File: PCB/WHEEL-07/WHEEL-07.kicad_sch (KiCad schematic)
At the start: 26 parts, among them J1 Conn_01x06_Male, J11 DBG, U1 STM32F405RGTx, Y1 16Mhz, Y2 32KHz

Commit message: Changed connectors setup
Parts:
- removed Y1: 16Mhz, Crystal:Crystal_SMD_5032-2Pin_5.0x3.2mm, symbol Device:Crystal_Small
- added H1, H2, H3, H4: MountingHole, MountingHole:MountingHole_2.2mm_M2, symbol Mechanical:MountingHole
- added Y1: 16Mhz, Crystal:Crystal_SMD_2016-4Pin_2.0x1.6mm, symbol Device:Crystal_GND24_Small
- C1, C2, C3, C34, C35, C36, C37, C4, C5, C6, C7, C8: footprint Capacitor_SMD:C_0402_1005Metric -> Capacitor_SMD:C_0402_1005Metric_Pad0.74x0.62mm_HandSolder
- C33: footprint Capacitor_SMD:C_0201_0603Metric -> Capacitor_SMD:C_0603_1608Metric
- L1: footprint (none) -> Inductor_SMD:L_0402_1005Metric
- R1, R2, R3, R5: footprint Resistor_SMD:R_0402_1005Metric -> Resistor_SMD:R_0402_1005Metric_Pad0.72x0.64mm_HandSolder
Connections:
- net CAN1_TERMINATOR_SW: now also U1.56 (PB4); no longer U1.59 (PB7)
- net CAN2_TERMINATOR_SW: now also U1.59 (PB7); no longer U1.56 (PB4)
- net GND: now also Y1.2, Y1.4
- net OSC_IN: now also Y1.1
- net OSC_OUT: now also Y1.3
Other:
- note added: "39uH"

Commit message: Finished layout
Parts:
- removed H2, H3, H4: MountingHole, MountingHole:MountingHole_2.2mm_M2, symbol Mechanical:MountingHole
- J1: footprint (none) -> Connector_Molex:Molex_Micro-Latch_53254-0670_1x06_P2.00mm_Horizontal
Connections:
- net CAN_BUS/CAN1_H: now also J1.3 (Pin_3); no longer J1.2 (Pin_2)
- net CAN_BUS/CAN1_L: now also J1.4 (Pin_4); no longer J1.1 (Pin_1)
- net CAN_BUS/CAN2_H: now also J1.5 (Pin_5); no longer J1.4 (Pin_4)
- net CAN_BUS/CAN2_L: now also J1.6 (Pin_6); no longer J1.3 (Pin_3)
- net GND: now also J1.1 (Pin_1); no longer J1.6 (Pin_6)
- net +12V: no longer names the net of J11.3 (Pin_3)
- net +12V: no longer J1.5 (Pin_5)
- net CAN1_TERMINATOR_SW: no longer names the net of U1.56 (PB4)
- net CAN2_TERMINATOR_SW: no longer names the net of U1.59 (PB7)
- new net 12V_CONN: J1.2 (Pin_2)
- no-connect marks 7 -> 11
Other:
- sheet CAN_BUS ports: added none; removed CAN_TERMINATOR_1, CAN_TERMINATOR_2

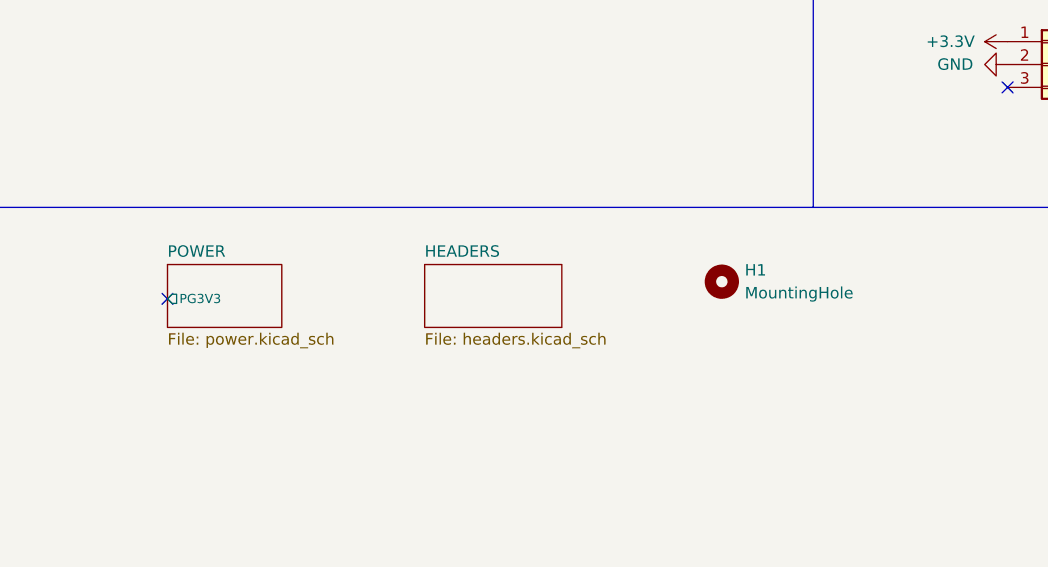
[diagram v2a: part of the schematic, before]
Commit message: Changed power supply section for 2 x LDO40
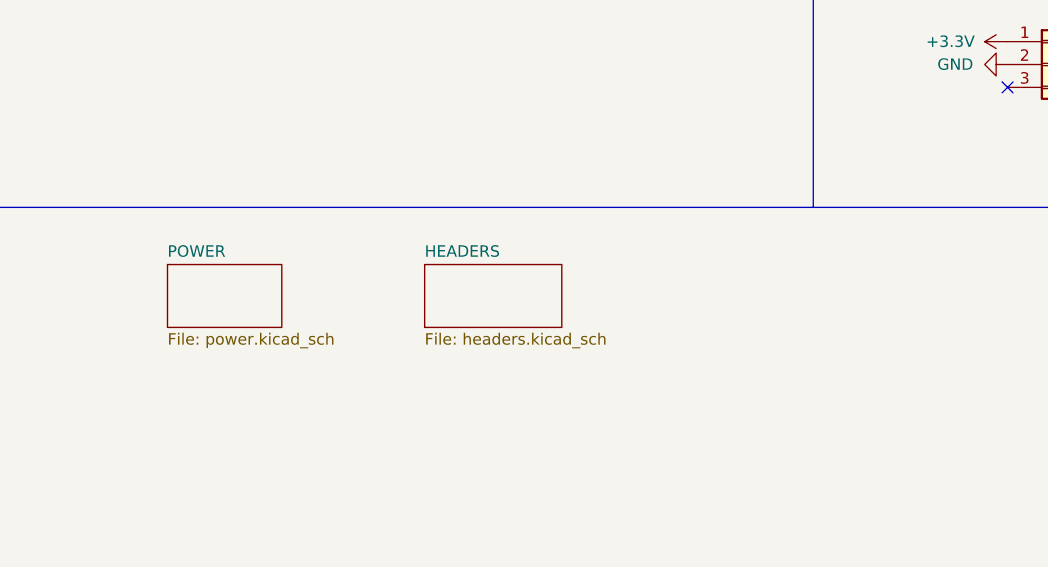
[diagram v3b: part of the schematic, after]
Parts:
- removed H1: MountingHole, MountingHole:MountingHole_2.2mm_M2, symbol Mechanical:MountingHole
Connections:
- no-connect marks 11 -> 10
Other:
- sheet POWER ports: added none; removed PG3V3

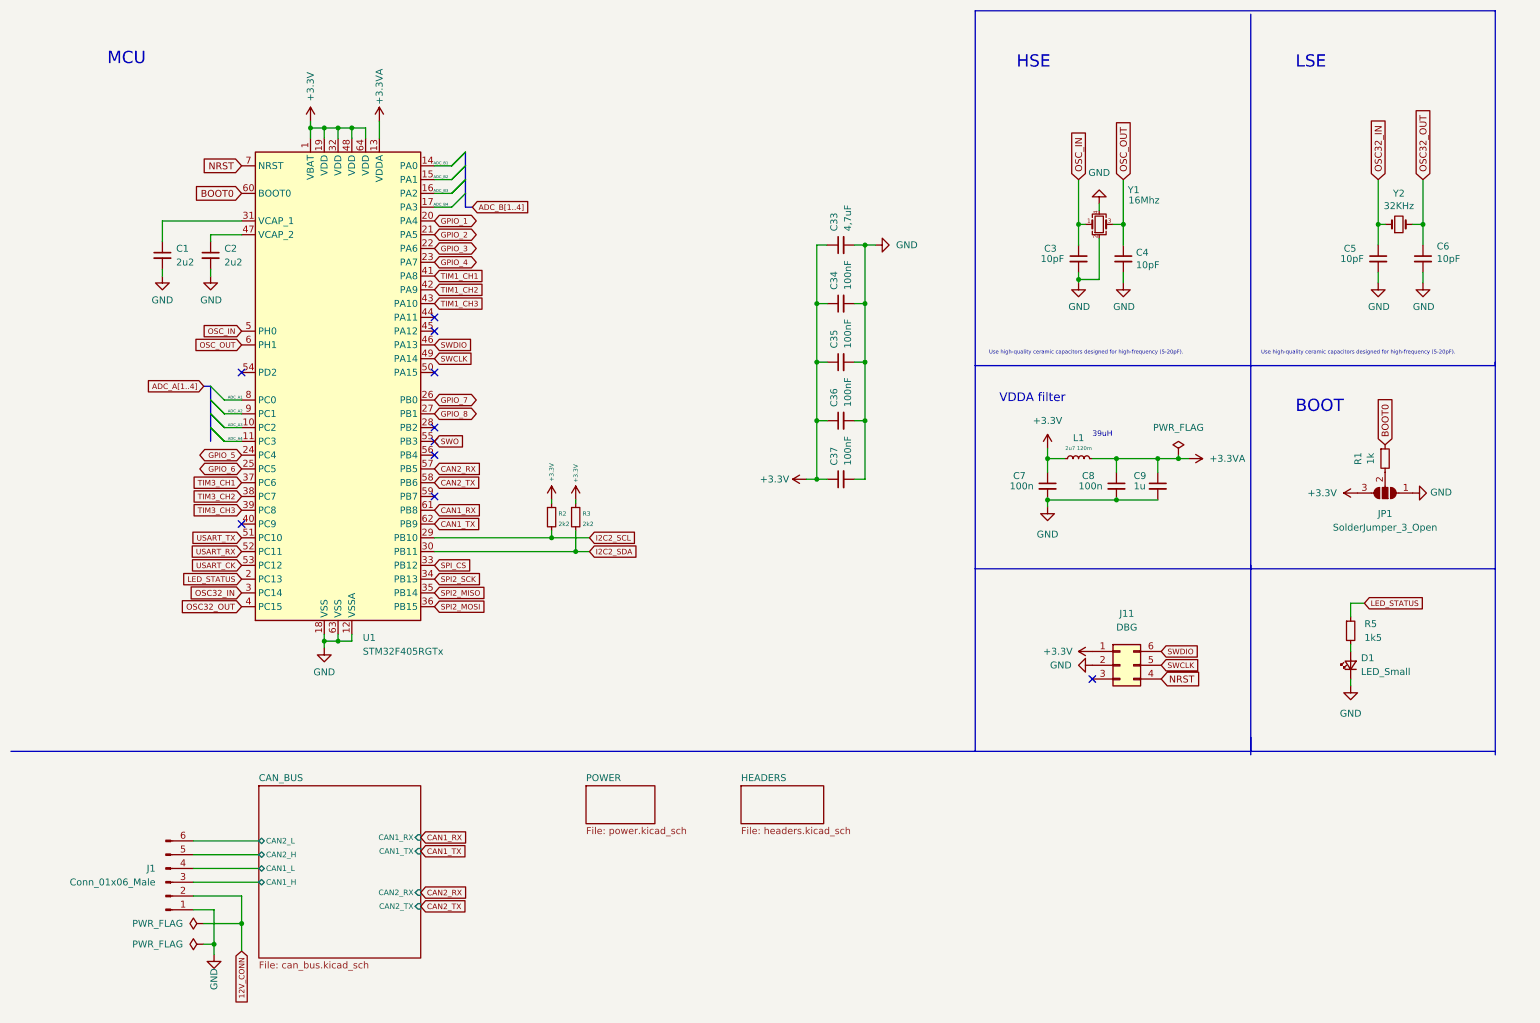
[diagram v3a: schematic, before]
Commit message: Revised board with 2 x LDO40 and cleaned-up schematics
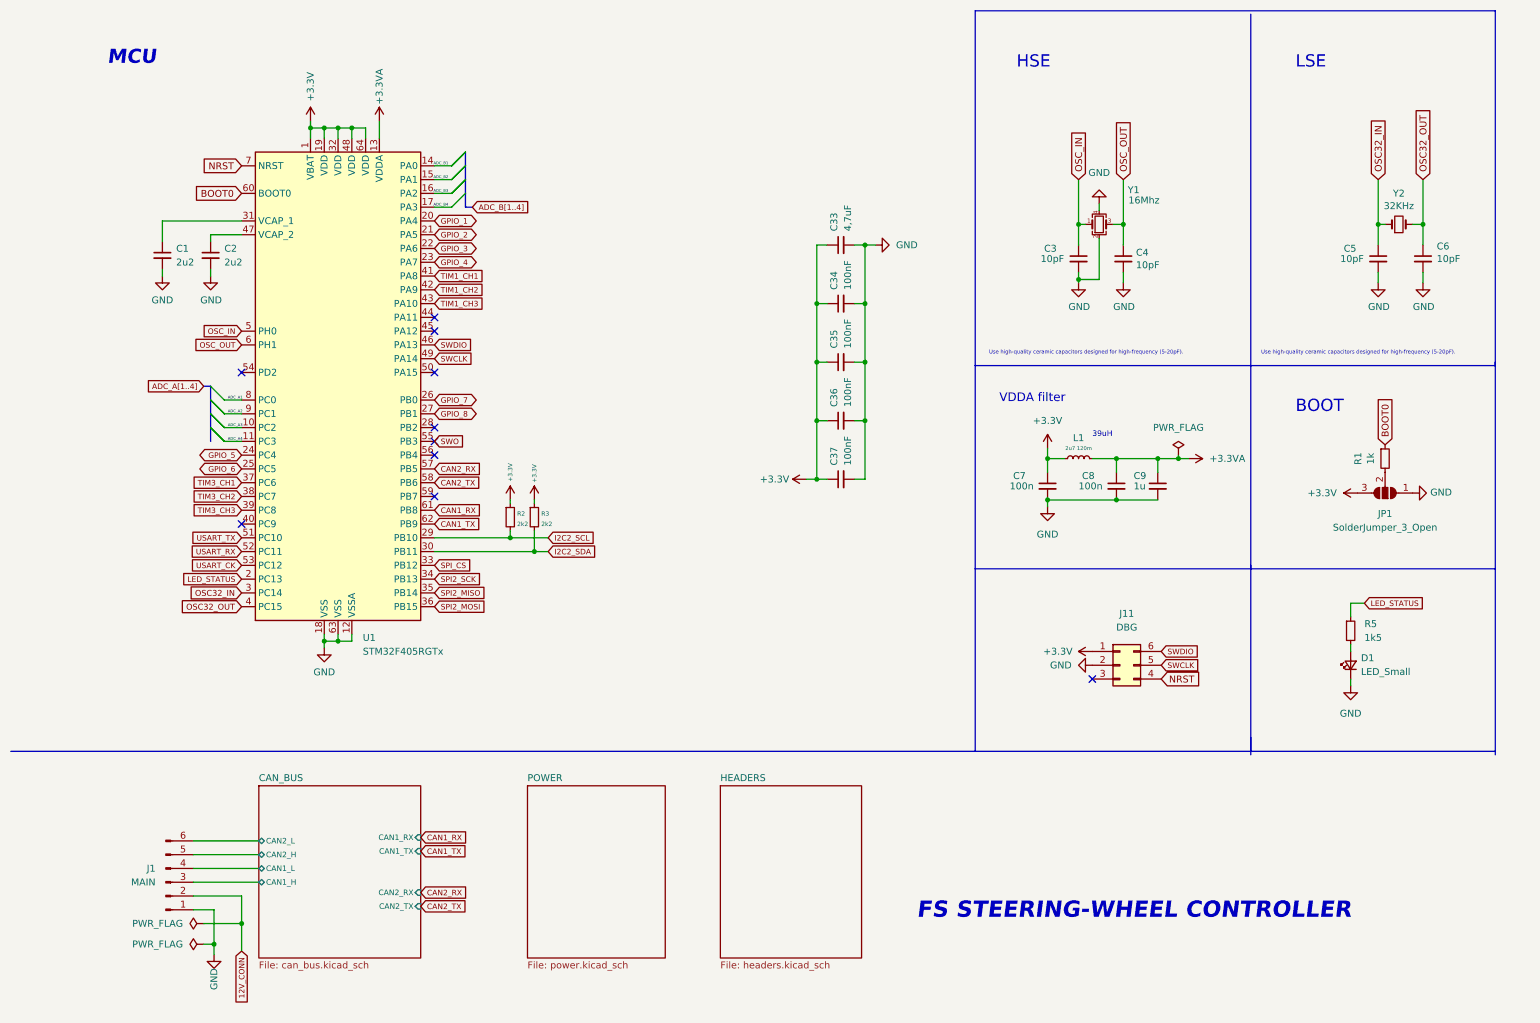
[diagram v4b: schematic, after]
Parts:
- J1: value Conn_01x06_Male -> MAIN
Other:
- note added: "FS STEERING-WHEEL CONTROLLER"
- moved on the sheet: R2, R3
